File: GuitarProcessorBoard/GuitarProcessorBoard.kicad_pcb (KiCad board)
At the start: 4 copper layers, 86 x 65 mm, 126 parts, among them J301 SWD Header, J302 PWR, J304 MODE, J305 BYP, J307 ScopeGroundLoop, SW301 RST, SW302 BOOT, U1 AMS1117, U201 TLV320AIC3204, U202 TL074, U301 STM32H7B0VBT6, U302 TPS63070, U303 SSD1306_OLED_128x64, U304 74HC595, Y301 32MHz, Y302 32.768kHZ

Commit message: rev2 sent to fab
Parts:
- moved SW302 2.27 mm to (-162.4, 44.5)
- moved C211 0.55 mm to (-126.5, 52.1)
- moved C210 0.33 mm to (-122.9, 51.9)
- moved R206 0.25 mm to (-126.5, 48.0)
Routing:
- net BOOT0: track 11.1 -> 8.92 mm
- net +3.3V: track 353.2 -> 354.6 mm
- net Net-(U201-AVDD): track 2.54 -> 3.30 mm
- net Net-(U201-IN1_L): track 15.3 -> 14.7 mm
- net /MCU/LED_A6: track 18.8 -> 18.2 mm
- net GND: track 95.6 -> 95.2 mm, vias 92 -> 98

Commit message: new layout
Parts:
- removed C201, C208, C209, C210, C211, C214, C215, C216, C304, C306, C307, C309, C311, C312, C313, C318, C322, C332, C333: 100n, Capacitor_SMD:C_0805_2012Metric
- removed C202, C308, C310, C314: 2u2, Capacitor_SMD:C_0805_2012Metric
- removed C203, C204, C205, C206, C303, C319, C321, C323: 10u, Capacitor_SMD:C_0805_2012Metric
- removed C207, C212: 4n7, Capacitor_SMD:C_0805_2012Metric
- removed C301, C302: 10p, Capacitor_SMD:C_0805_2012Metric
- removed C315, C317: 6p, Capacitor_SMD:C_0805_2012Metric
- removed C324: 22u, Capacitor_SMD:C_0805_2012Metric
- removed C326: 330u, Capacitor_THT:CP_Radial_D5.0mm_P2.50mm
- removed C327, C328, C329: 10n, Capacitor_SMD:C_0805_2012Metric
- removed D301: RED, LED_THT:LED_D3.0mm
- removed D302, D308, D309, D310, D311, D312: ORANGE, LED_THT:LED_D3.0mm
- removed D304: PMEG3030, Diode_SMD:D_SOD-123
- removed D307: GREEN, LED_THT:LED_D3.0mm
- removed J301: SWD Header, Connector_PinHeader_2.54mm:PinHeader_1x06_P2.54mm_Vertical
- removed J302: PWR, Connector_PinHeader_2.54mm:PinHeader_1x04_P2.54mm_Vertical
- removed J304: MODE, Connector_PinHeader_2.54mm:PinHeader_1x02_P2.54mm_Vertical
- removed J305: BYP, Connector_PinHeader_2.54mm:PinHeader_1x02_P2.54mm_Vertical
- removed J307: ScopeGroundLoop, Connector:THT_GND_WIRE
- removed L301: 1u5, Inductor_SMD:L_Coilcraft_XAL4020-XXX
- removed R201, R305, R313: 47k, Resistor_SMD:R_0805_2012Metric
- removed R202, R203, R205, R209, R210, R211, R215, R309, R310, R312, R327, R328: 100k, Resistor_SMD:R_0805_2012Metric
- removed R204, R212, R216: 51k, Resistor_SMD:R_0805_2012Metric
- removed R206, R207: 470k, Resistor_SMD:R_0805_2012Metric
- removed R208, R214: 1k, Resistor_SMD:R_0805_2012Metric
- removed R220, R330, R331, R332, R333: 22, Resistor_SMD:R_0805_2012Metric
- removed R301, R302, R303, R304: 2k2, Resistor_SMD:R_0805_2012Metric
- removed R306, R307, R308, R318, R322, R323, R324, R325: 470, Resistor_SMD:R_0805_2012Metric
- removed R311: 10k, Resistor_SMD:R_0805_2012Metric
- removed R314: 5k1, Resistor_SMD:R_0805_2012Metric
- removed R315, R316, R317: 22k, Resistor_SMD:R_0805_2012Metric
- removed RV301, RV302, RV303: 100kB, Potentiometer_THT:Potentiometer_Alpha_RD901F-40-00D_Single_Vertical_CircularHoles
- removed SW301: RST, Button_Switch_SMD:SW_SPST_B3U-1000P
- removed SW302: BOOT, Button_Switch_SMD:SW_SPST_B3U-1000P
- removed TP301: In, TestPoint:TestPoint_THTPad_D2.0mm_Drill1.0mm_VAL
- removed TP302: Out, TestPoint:TestPoint_THTPad_D2.0mm_Drill1.0mm_VAL
- removed TP303: 3v3D, TestPoint:TestPoint_THTPad_D2.0mm_Drill1.0mm_VAL
- removed U201: TLV320AIC3204, Package_DFN_QFN:VQFN-32-1EP_5x5mm_P0.5mm_EP3.1x3.1mm
- removed U202: TL074, Package_SO:SOIC-14_3.9x8.7mm_P1.27mm
- removed U301: STM32H7B0VBT6, Package_QFP:LQFP-100_14x14mm_P0.5mm
- removed U302: TPS63070, Package_DFN_QFN:TXN_QFN15
- removed U303: SSD1306_OLED_128x64, Display:SSD1306_OLED_128x64_OffBoard
- removed U304: 74HC595, Package_SO:SOIC-16_3.9x9.9mm_P1.27mm
- removed Y301: 32MHz, Crystal:Crystal_SMD_EuroQuartz_MT-4Pin_3.2x2.5mm
- removed Y302: 32.768kHZ, Crystal:Crystal_SMD_SeikoEpson_MC306-4Pin_8.0x3.2mm
- added C10: 10u, Capacitor_SMD:C_0805_2012Metric, B.Cu at (-142.6, 83.1)
- added C11: 10u, Capacitor_SMD:C_0805_2012Metric, B.Cu at (-142.4, 77.5)
- added C12: 10u, Capacitor_SMD:C_0805_2012Metric, B.Cu at (-165.9, 81.7)
- added C13: 10u, Capacitor_SMD:C_0805_2012Metric, B.Cu at (-137.8, 89.8)
- added C14: 100n, Capacitor_SMD:C_0805_2012Metric, B.Cu at (-143.9, 79.0)
- added C15: 4n7, Capacitor_SMD:C_0805_2012Metric, B.Cu at (-150.1, 80.4)
- added C16: 4n7, Capacitor_SMD:C_0805_2012Metric, B.Cu at (-144.3, 86.9)
- added C17: 2u2, Capacitor_SMD:C_0805_2012Metric, B.Cu at (-139.1, 79.6)
- added C18: 100n, Capacitor_SMD:C_0805_2012Metric, B.Cu at (-146.9, 89.4)
- added C19: 100n, Capacitor_SMD:C_0805_2012Metric, B.Cu at (-151.2, 84.6)
- added C20: 10u, Capacitor_SMD:C_0805_2012Metric, B.Cu at (-130.1, 84.8)
- added C21: 1u, Capacitor_SMD:C_0805_2012Metric, B.Cu at (-150.9, 95.3)
- added C22: 1u, Capacitor_SMD:C_0805_2012Metric, B.Cu at (-162.0, 90.6)
- added C24: 10p, Capacitor_SMD:C_0805_2012Metric, B.Cu at (-119.9, 51.8)
- added C25: 10u, Capacitor_SMD:C_0805_2012Metric, B.Cu at (-173.0, 70.4)
- added C26: 10p, Capacitor_SMD:C_0805_2012Metric, B.Cu at (-124.2, 47.9)
- added C27: 100n, Capacitor_SMD:C_0805_2012Metric, B.Cu at (-153.8, 74.6)
- added C28: 100n, Capacitor_SMD:C_0805_2012Metric, B.Cu at (-127.5, 50.3)
- added C29: 100n, Capacitor_SMD:C_0805_2012Metric, B.Cu at (-130.0, 48.1)
- added C30: 100n, Capacitor_SMD:C_0805_2012Metric, B.Cu at (-147.1, 60.1)
- added C31: 2u2, Capacitor_SMD:C_0805_2012Metric, B.Cu at (-130.4, 72.0)
- added C32: 100n, Capacitor_SMD:C_0805_2012Metric, B.Cu at (-134.7, 72.1)
- added C33: 2u2, Capacitor_SMD:C_0805_2012Metric, B.Cu at (-146.3, 64.4)
- added C34: 100n, Capacitor_SMD:C_0805_2012Metric, B.Cu at (-122.3, 61.6)
- added C35: 100n, Capacitor_SMD:C_0805_2012Metric, B.Cu at (-137.6, 48.1)
- added C36: 100n, Capacitor_SMD:C_0805_2012Metric, B.Cu at (-123.5, 54.8)
- added C37: 330u, Capacitor_THT:CP_Radial_D5.0mm_P2.50mm, B.Cu at (-94.8, 88.5)
- added C40: 100n, Capacitor_SMD:C_0805_2012Metric, B.Cu at (-92.0, 82.1)
- added C41: 330u, Capacitor_THT:CP_Radial_D5.0mm_P2.50mm, B.Cu at (-119.6, 57.9)
- added C42: 100n, Capacitor_SMD:C_0805_2012Metric, B.Cu at (-92.0, 78.4)
- added C43: 1u, Capacitor_SMD:C_0805_2012Metric, B.Cu at (-109.0, 80.6)
- added C44: 10u, Capacitor_SMD:C_0805_2012Metric, B.Cu at (-102.2, 74.9)
- added C45: 10n, Capacitor_SMD:C_0805_2012Metric, B.Cu at (-157.0, 41.8)
- added C46: 10n, Capacitor_SMD:C_0805_2012Metric, B.Cu at (-113.5, 41.5)
- added C47: 10u, Capacitor_SMD:C_0805_2012Metric, B.Cu at (-167.5, 47.7)
- added C48: 10n, Capacitor_SMD:C_0805_2012Metric, B.Cu at (-106.2, 68.2)
- added C49: 10n, Capacitor_SMD:C_0805_2012Metric, B.Cu at (-135.4, 41.7)
- added C50: 10u, Capacitor_SMD:C_0805_2012Metric, B.Cu at (-167.6, 44.2)
- added C51: 100n, Capacitor_SMD:C_0805_2012Metric, B.Cu at (-175.3, 39.8)
- added C53: 10u, Capacitor_SMD:C_0805_2012Metric, B.Cu at (-168.3, 37.2)
- added C54: 22u, Capacitor_SMD:C_0805_2012Metric, B.Cu at (-168.3, 33.9)
- added C55: 330u, Capacitor_THT:CP_Radial_D5.0mm_P2.50mm, B.Cu at (-176.4, 47.0)
- added C56: 330u, Capacitor_THT:CP_Radial_D5.0mm_P2.50mm, B.Cu at (-108.9, 47.5)
- added C8: 100n, Capacitor_SMD:C_0805_2012Metric, B.Cu at (-114.0, 91.6)
- added C9: 10u, Capacitor_SMD:C_0805_2012Metric, B.Cu at (-112.6, 80.6)
- added D1: PMEG3030, Diode_SMD:D_SOD-123, B.Cu at (-97.7, 90.3)
- added D2: RED, LED_THT:LED_D3.0mm, F.Cu at (-144.0, 35.9)
- added D3: GREEN, LED_THT:LED_D3.0mm, F.Cu at (-122.2, 35.8)
- added D4: ORANGE, LED_THT:LED_D3.0mm, F.Cu at (-92.0, 36.2)
- added D5: ORANGE, LED_THT:LED_D3.0mm, F.Cu at (-92.0, 42.7)
- added D6: ORANGE, LED_THT:LED_D3.0mm, F.Cu at (-92.0, 49.2)
- added D7: ORANGE, LED_THT:LED_D3.0mm, F.Cu at (-92.0, 55.7)
- added D8: ORANGE, LED_THT:LED_D3.0mm, F.Cu at (-92.0, 62.2)
- added D9: ORANGE, LED_THT:LED_D3.0mm, F.Cu at (-92.0, 68.7)
- added J1: SWD Header, Connector_PinHeader_2.54mm:PinHeader_1x06_P2.54mm_Vertical, F.Cu at (-176.0, 54.3)
- added J2: IO, Connector_PinHeader_2.54mm:PinHeader_1x06_P2.54mm_Vertical, F.Cu at (-107.8, 98.1)
- added J3: ScopeGroundLoop, Capacitor_THT:THT_GND_WIRE, B.Cu at (-101.6, 37.4)
- added J4: MODE, Connector_PinHeader_2.54mm:PinHeader_1x02_P2.54mm_Vertical, B.Cu at (-176.1, 94.8)
- added J5: BYP, Connector_PinHeader_2.54mm:PinHeader_1x02_P2.54mm_Vertical, B.Cu at (-176.2, 87.0)
- added L1: 1u5, Inductor_SMD:L_Coilcraft_XAL4020-XXX, B.Cu at (-166.9, 40.7)
- added R1: 470k, Resistor_SMD:R_0805_2012Metric, B.Cu at (-117.7, 84.7)
- added R10: 22, Resistor_SMD:R_0805_2012Metric, B.Cu at (-130.7, 81.5)
- added R11: 100k, Resistor_SMD:R_0805_2012Metric, B.Cu at (-109.0, 77.3)
- added R12: 100k, Resistor_SMD:R_0805_2012Metric, B.Cu at (-112.6, 77.3)
- added R13: 100k, Resistor_SMD:R_0805_2012Metric, B.Cu at (-164.3, 83.2)
- added R14: 100k, Resistor_SMD:R_0805_2012Metric, B.Cu at (-161.8, 80.7)
- added R15: 1k, Resistor_SMD:R_0805_2012Metric, B.Cu at (-148.7, 81.9)
- added R16: 1k, Resistor_SMD:R_0805_2012Metric, B.Cu at (-145.8, 85.5)
- added R17: 470k, Resistor_SMD:R_0805_2012Metric, B.Cu at (-150.1, 91.3)
- added R18: 470k, Resistor_SMD:R_0805_2012Metric, B.Cu at (-158.5, 84.0)
- added R19: 470k, Resistor_SMD:R_0805_2012Metric, B.Cu at (-152.6, 93.8)
- added R2: 470k, Resistor_SMD:R_0805_2012Metric, B.Cu at (-110.9, 89.1)
- added R20: 470k, Resistor_SMD:R_0805_2012Metric, B.Cu at (-161.0, 86.5)
- added R21: 100k, Resistor_SMD:R_0805_2012Metric, B.Cu at (-167.8, 65.9)
- added R22: 100k, Resistor_SMD:R_0805_2012Metric, B.Cu at (-139.9, 50.6)
- added R23: 47k, Resistor_SMD:R_0805_2012Metric, B.Cu at (-159.0, 65.2)
- added R26: 22, Resistor_SMD:R_0805_2012Metric, B.Cu at (-121.6, 70.5)
- added R27: 22, Resistor_SMD:R_0805_2012Metric, B.Cu at (-114.1, 67.0)
- added R28: 22, Resistor_SMD:R_0805_2012Metric, B.Cu at (-118.1, 68.6)
- added R29: 22, Resistor_SMD:R_0805_2012Metric, B.Cu at (-115.1, 72.1)
- added R3: 470k, Resistor_SMD:R_0805_2012Metric, B.Cu at (-119.4, 97.3)
- added R30: 2k2, Resistor_SMD:R_0805_2012Metric, B.Cu at (-125.6, 82.5)
- added R31: 2k2, Resistor_SMD:R_0805_2012Metric, B.Cu at (-122.2, 83.5)
- added R32: 100k, Resistor_SMD:R_0805_2012Metric, B.Cu at (-172.4, 96.5)
- added R33: 100k, Resistor_SMD:R_0805_2012Metric, B.Cu at (-172.6, 88.6)
- added R34: 22k, Resistor_SMD:R_0805_2012Metric, B.Cu at (-154.6, 41.7)
- added R35: 22k, Resistor_SMD:R_0805_2012Metric, B.Cu at (-111.4, 41.6)
- added R36: 22k, Resistor_SMD:R_0805_2012Metric, B.Cu at (-104.1, 68.2)
- added R37: 22k, Resistor_SMD:R_0805_2012Metric, B.Cu at (-132.9, 41.7)
- added R38: 10k, Resistor_SMD:R_0805_2012Metric, B.Cu at (-171.2, 44.2)
- added R39: 47k, Resistor_SMD:R_0805_2012Metric, B.Cu at (-170.1, 78.4)
- added R4: 470k, Resistor_SMD:R_0805_2012Metric, B.Cu at (-110.8, 94.3)
- added R42: 100k, Resistor_SMD:R_0805_2012Metric, B.Cu at (-175.3, 42.1)
- added R43: 47k, Resistor_SMD:R_0805_2012Metric, B.Cu at (-172.0, 36.5)
- added R44: 15k, Resistor_SMD:R_0805_2012Metric, B.Cu at (-175.4, 36.5)
- added R45: 470, Resistor_SMD:R_0805_2012Metric, B.Cu at (-144.0, 41.7)
- added R46: 470, Resistor_SMD:R_0805_2012Metric, B.Cu at (-122.2, 41.4)
- added R47: 470, Resistor_SMD:R_0805_2012Metric, B.Cu at (-97.6, 36.2)
- added R48: 470, Resistor_SMD:R_0805_2012Metric, B.Cu at (-97.6, 42.5)
- added R49: 470, Resistor_SMD:R_0805_2012Metric, B.Cu at (-97.6, 49.6)
- added R5: 470k, Resistor_SMD:R_0805_2012Metric, B.Cu at (-124.6, 88.9)
- added R50: 470, Resistor_SMD:R_0805_2012Metric, B.Cu at (-97.6, 55.8)
- added R51: 470, Resistor_SMD:R_0805_2012Metric, B.Cu at (-97.8, 60.7)
- added R52: 470, Resistor_SMD:R_0805_2012Metric, B.Cu at (-97.8, 68.7)
- added R6: 470k, Resistor_SMD:R_0805_2012Metric, B.Cu at (-113.8, 88.4)
- added R7: 470k, Resistor_SMD:R_0805_2012Metric, B.Cu at (-124.5, 95.1)
- added R8: 470k, Resistor_SMD:R_0805_2012Metric, B.Cu at (-113.6, 95.2)
- added R9: 47k, Resistor_SMD:R_0805_2012Metric, B.Cu at (-134.2, 77.0)
- added RV1: 100kB, Potentiometer_THT:Potentiometer_Alpha_RD901F-40-00D_Single_Vertical_CircularHoles, F.Cu at (-157.1, 44.6)
- added RV2: 100kB, Potentiometer_THT:Potentiometer_Alpha_RD901F-40-00D_Single_Vertical_CircularHoles, F.Cu at (-113.9, 44.6)
- added RV3: 100kB, Potentiometer_THT:Potentiometer_Alpha_RD901F-40-00D_Single_Vertical_CircularHoles, F.Cu at (-106.5, 71.3)
- added RV4: 100kB, Potentiometer_THT:Potentiometer_Alpha_RD901F-40-00D_Single_Vertical_CircularHoles, F.Cu at (-135.5, 44.6)
- added SW1: RST, Button_Switch_SMD:SW_SPST_B3U-1000P, B.Cu at (-167.1, 63.2)
- added SW3: SW_1, Button_Switch_THT:MiniToggle_SPST, F.Cu at (-174.0, 75.9)
- added TP10: DACR, TestPoint:TestPoint_THTPad_D2.0mm_Drill1.0mm_VAL, B.Cu at (-154.2, 81.1)
- added TP2: InR, TestPoint:TestPoint_THTPad_D2.0mm_Drill1.0mm_VAL, B.Cu at (-100.5, 87.0)
- added TP3: 3v3D, TestPoint:TestPoint_THTPad_D2.0mm_Drill1.0mm_VAL, B.Cu at (-168.9, 54.2)
- added TP4: OutL, TestPoint:TestPoint_THTPad_D2.0mm_Drill1.0mm_VAL, B.Cu at (-146.4, 94.6)
- added TP5: OutR, TestPoint:TestPoint_THTPad_D2.0mm_Drill1.0mm_VAL, B.Cu at (-162.6, 95.4)
- added TP6: 3v3A, TestPoint:TestPoint_THTPad_D2.0mm_Drill1.0mm_VAL, B.Cu at (-105.2, 80.6)
- added TP7: DB1, TestPoint:TestPoint_THTPad_D2.0mm_Drill1.0mm_VAL, B.Cu at (-147.8, 55.6)
- added TP8: DB2, TestPoint:TestPoint_THTPad_D2.0mm_Drill1.0mm_VAL, B.Cu at (-144.8, 53.5)
- added TP9: DACL, TestPoint:TestPoint_THTPad_D2.0mm_Drill1.0mm_VAL, B.Cu at (-142.4, 90.4)
- added U2: TL072, Package_SO:SOIC-8_3.9x4.9mm_P1.27mm, B.Cu at (-156.8, 89.2)
- added U3: TLV320AIC3204, Package_DFN_QFN:VQFN-32-1EP_5x5mm_P0.5mm_EP3.1x3.1mm, B.Cu at (-136.4, 85.2)
- added U4: 74HC595, Package_SO:SOIC-16_3.9x9.9mm_P1.27mm, B.Cu at (-160.8, 71.4)
- added U5: STM32H7B0VBT6, Package_QFP:LQFP-100_14x14mm_P0.5mm, B.Cu at (-134.5, 60.2)
- added U6: AMS1117, Package_TO_SOT_SMD:SOT-223-3_TabPin2, B.Cu at (-98.8, 80.4)
- added U7: TPS63070, Converter_DCDC:TXN_QFN15, B.Cu at (-171.3, 40.7)
- added Y1: 32MHz, Crystal:Crystal_SMD_EuroQuartz_MT-4Pin_3.2x2.5mm, B.Cu at (-122.1, 49.9)
- C1, C3: value 330u -> 100n; footprint Capacitor_THT:CP_Radial_D5.0mm_P2.50mm -> Capacitor_SMD:C_0805_2012Metric
- C2, C7: value 10u -> 100n
- C6: value 1u -> 100n
- TP1: value 3v3A -> InL; moved to B.Cu
- U1: value AMS1117 -> TL074; footprint Package_TO_SOT_SMD:SOT-223-3_TabPin2 -> Package_SO:SOIC-14_3.9x8.7mm_P1.27mm
- moved C7 79.1 mm to (-157.1, 94.4), turned to -45 degrees
- moved C1 68.6 mm to (-105.5, 87.0)
- moved C5 63.3 mm to (-130.8, 92.4), turned to 180 degrees
- moved C4 62.2 mm to (-129.1, 88.1), turned to 180 degrees
- moved C6 59.5 mm to (-130.8, 94.6), turned to 180 degrees
- moved U1 57.5 mm to (-119.7, 91.6), turned to 180 degrees
- moved C2 52.4 mm to (-105.6, 89.7)
- moved TP1 46.2 mm to (-102.2, 89.8), turned to 180 degrees
- moved C3 37.6 mm to (-129.1, 90.2)
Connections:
- C1 pad 1: +3.3V -> IN_R
- C1 pad 2: GND -> Net-(C1-Pad2)
- C2 pad 1: +3.3VA -> IN_L
- C2 pad 2: GND -> Net-(C2-Pad2)
- C3 pad 1: +3.3VA -> /Audio/RightInputNeg
- C3 pad 2: GND -> /Audio/In1R
- C4 pad 1: GND -> /Audio/RightInputPos
- C4 pad 2: VCC -> /Audio/In1L
- C5 pad 1: GND -> /Audio/LeftInputNeg
- C5 pad 2: +3.3VA -> /Audio/In2L
- C6 pad 1: +3.3VA -> /Audio/LeftInputPos
- C6 pad 2: GND -> /Audio/In2R
- C7 pad 1: +3.3VA -> VCC
- TP1 pad 1: +3.3VA -> IN_L
- U1 pad 1: GND -> /Audio/RightInputPos
- U1 pad 2: +3.3VA -> Net-(U1A--)
- U1 pad 3: VCC -> /Audio/Bias1
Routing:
- net +3.3V: track 354.6 -> 0.00 mm, vias 5 -> 0
- net VCC: track 196.9 -> 0.00 mm, vias 1 -> 0
- net +3.3VA: track 161.5 -> 0.00 mm, vias 5 -> 0
- net ADC_C: track 109.1 -> 0.00 mm, vias 2 -> 0
- net GND: track 95.2 -> 0.00 mm, vias 98 -> 0
- net FX_IN: track 85.8 -> 0.00 mm, vias 3 -> 0
- net LED_DATA: track 79.0 -> 0.00 mm, vias 1 -> 0
- net ADC_B: track 75.1 -> 0.00 mm, vias 2 -> 0
- net LED_NRST: track 73.3 -> 0.00 mm, vias 1 -> 0
- net FX_OUT: track 73.0 -> 0.00 mm, vias 2 -> 0
- net LED_LATCH: track 71.3 -> 0.00 mm, vias 1 -> 0
- net LED_SCK: track 68.6 -> 0.00 mm, vias 1 -> 0
- net NRST: track 64.4 -> 0.00 mm, vias 1 -> 0
- net /MCU/LED_BYPASS: track 62.3 -> 0.00 mm
- net BYP_BTN: track 54.8 -> 0.00 mm, vias 1 -> 0
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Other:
- board size 86 x 65 mm -> 88.7 x 70 mm
- board text added: "INL"
- board text added: "INR"
- board text added: "OUTL"
- board text added: "OUTR"
- board text added: "Rev 3- 04/2026 Hayden Setlik"
- board text removed: "Bypass"
- board text removed: "IN"
- board text removed: "OUT"
- board text removed: "Rev 2- 01/2026 Hayden Setlik"
- board text removed: "Tempo"

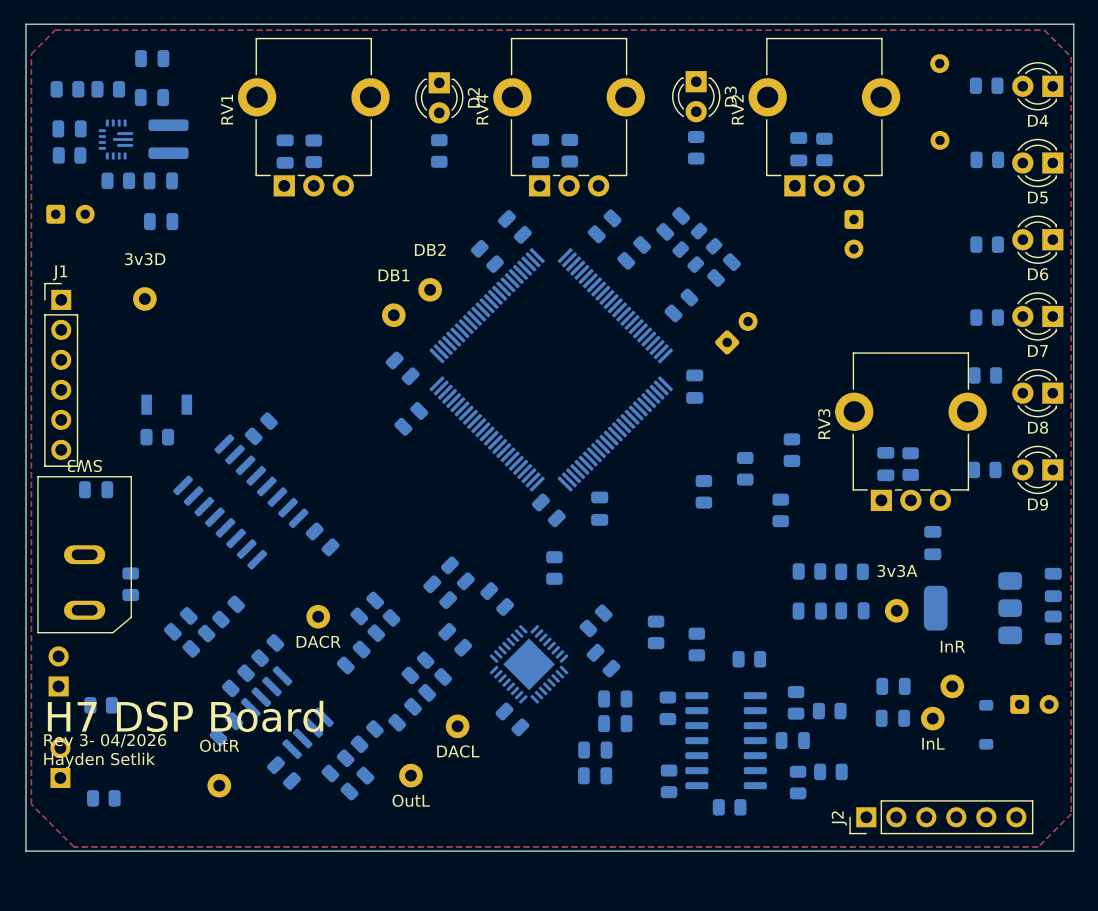
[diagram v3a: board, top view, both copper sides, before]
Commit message: prelim. routing, DRC passing
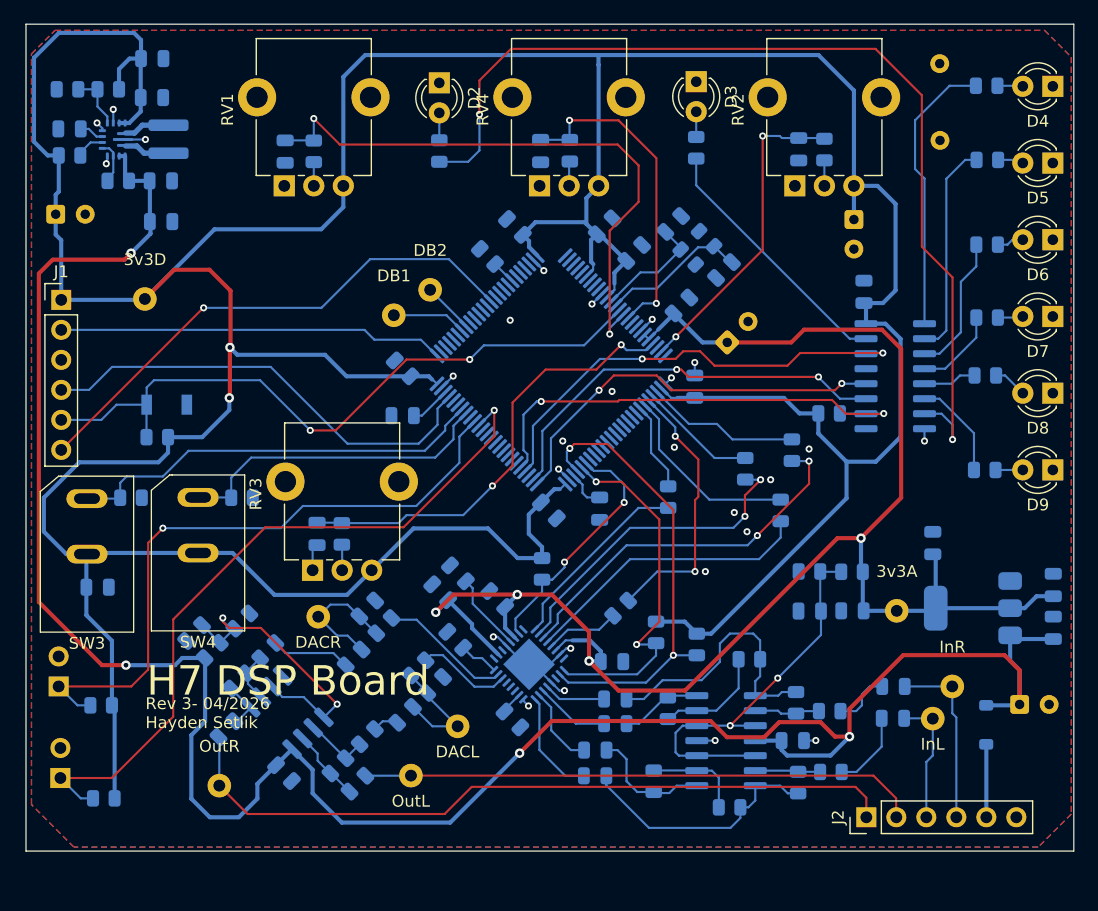
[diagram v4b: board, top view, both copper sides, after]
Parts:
- added R40: 47k, Resistor_SMD:R_0805_2012Metric, B.Cu at (-160.7, 71.0)
- added SW4: SW_2, Button_Switch_THT:MiniToggle_SPST, F.Cu at (-164.4, 75.7)
- moved U4 56.4 mm to (-105.4, 60.8), turned to 180 degrees
- moved C27 50.4 mm to (-108.0, 53.6), turned to 90 degrees
- moved C48 48.5 mm to (-154.3, 74.1)
- moved R36 48.5 mm to (-152.2, 74.1)
- moved RV3 48.5 mm to (-154.7, 77.2)
- moved R23 48.1 mm to (-111.0, 63.9), turned to 0 degrees
- moved C25 8.25 mm to (-172.9, 78.6)
- moved R39 7.33 mm to (-170.1, 71.0), turned to 0 degrees
- moved R26 3.06 mm to (-124.6, 71.0)
- moved R10 2.34 mm to (-128.6, 80.4)
- moved C12 1.37 mm to (-164.7, 82.5)
- moved R13 1.37 mm to (-163.2, 84.0)
- moved R14 1.37 mm to (-160.7, 81.5)
- moved R7 1.30 mm to (-125.8, 95.0), turned to 90 degrees
- moved R9 1.05 mm to (-135.3, 77.1)
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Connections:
- J2 pad 1: OUT_L -> OUT_R
- J2 pad 2: OUT_R -> OUT_L
- R7 pad 1: Net-(U1C--) -> /Audio/LeftInputNeg
- R7 pad 2: /Audio/LeftInputNeg -> Net-(U1C--)
- R9 pad 1: +3.3VA -> +3.3V
- U4 pad 1: /MCU/LED_A5 -> /MCU/LED_A1
- U4 pad 15: /MCU/LED_A6 -> /MCU/LED_BYPASS
- U4 pad 2: /MCU/LED_A4 -> /MCU/LED_A2
- U4 pad 4: /MCU/LED_A2 -> /MCU/LED_A4
- U4 pad 5: /MCU/LED_A1 -> /MCU/LED_A5
- U4 pad 6: /MCU/LED_BYPASS -> /MCU/LED_A6
- U5 pad 53: LED_NRST -> unconnected-(U5-PB14-Pad53)
- U5 pad 55: unconnected-(U5-PD8-Pad55) -> LED_NRST
- U5 pad 65: unconnected-(U5-PC8-Pad65) -> MODE_BTN
- U5 pad 66: SWITCH1 -> BYP_BTN
- U5 pad 68: BYP_BTN -> SWITCH2
- U5 pad 69: MODE_BTN -> SWITCH1
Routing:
- net +3.3V: track 0.00 -> 389.8 mm, vias 0 -> 2
- net VCC: track 0.00 -> 189.5 mm, vias 0 -> 4
- net +3.3VA: track 0.00 -> 135.3 mm, vias 0 -> 4
- net /MCU/LED_TEMPO: track 0.00 -> 84.1 mm, vias 0 -> 2
- net OUT_R: track 0.00 -> 62.9 mm
- net MODE_BTN: track 0.00 -> 61.1 mm, vias 0 -> 1
- net NRST: track 0.00 -> 58.2 mm, vias 0 -> 2
- net BYP_BTN: track 0.00 -> 55.4 mm, vias 0 -> 1
- net ADC_C: track 0.00 -> 50.9 mm, vias 0 -> 2
- net OUT_L: track 0.00 -> 47.3 mm
- net SWO: track 0.00 -> 44.6 mm, vias 0 -> 1
- net LED_NRST: track 0.00 -> 40.1 mm, vias 0 -> 2
- net SWDIO: track 0.00 -> 38.8 mm
- net CODEC_SDA: track 0.00 -> 38.8 mm, vias 0 -> 2
- net LED_DATA: track 0.00 -> 38.8 mm, vias 0 -> 2
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
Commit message: minor tweaks
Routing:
- net GND: track 31.7 -> 36.9 mm, vias 27 -> 31
- net OUT_R: track 62.9 -> 60.0 mm
- net ADC_C: track 50.9 -> 52.6 mm

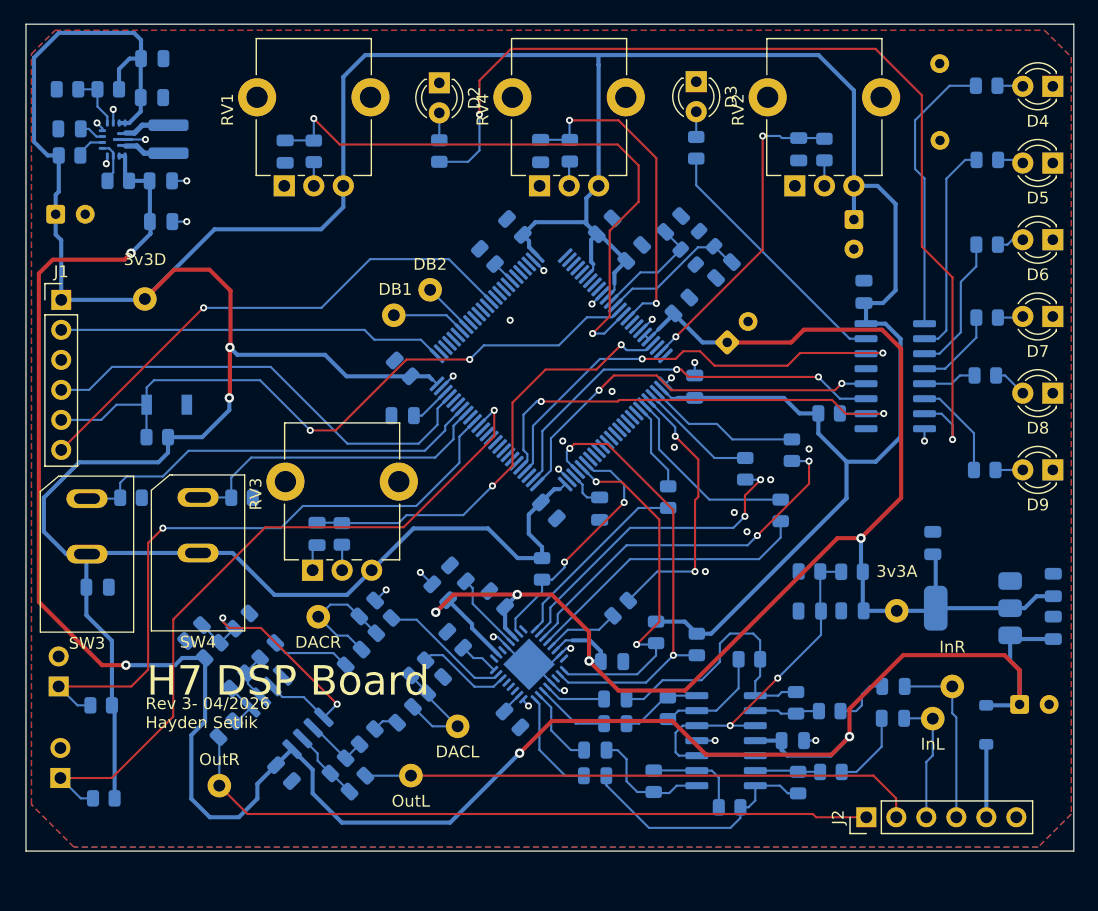
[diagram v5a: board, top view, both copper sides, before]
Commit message: new layout, pinout switcharoo
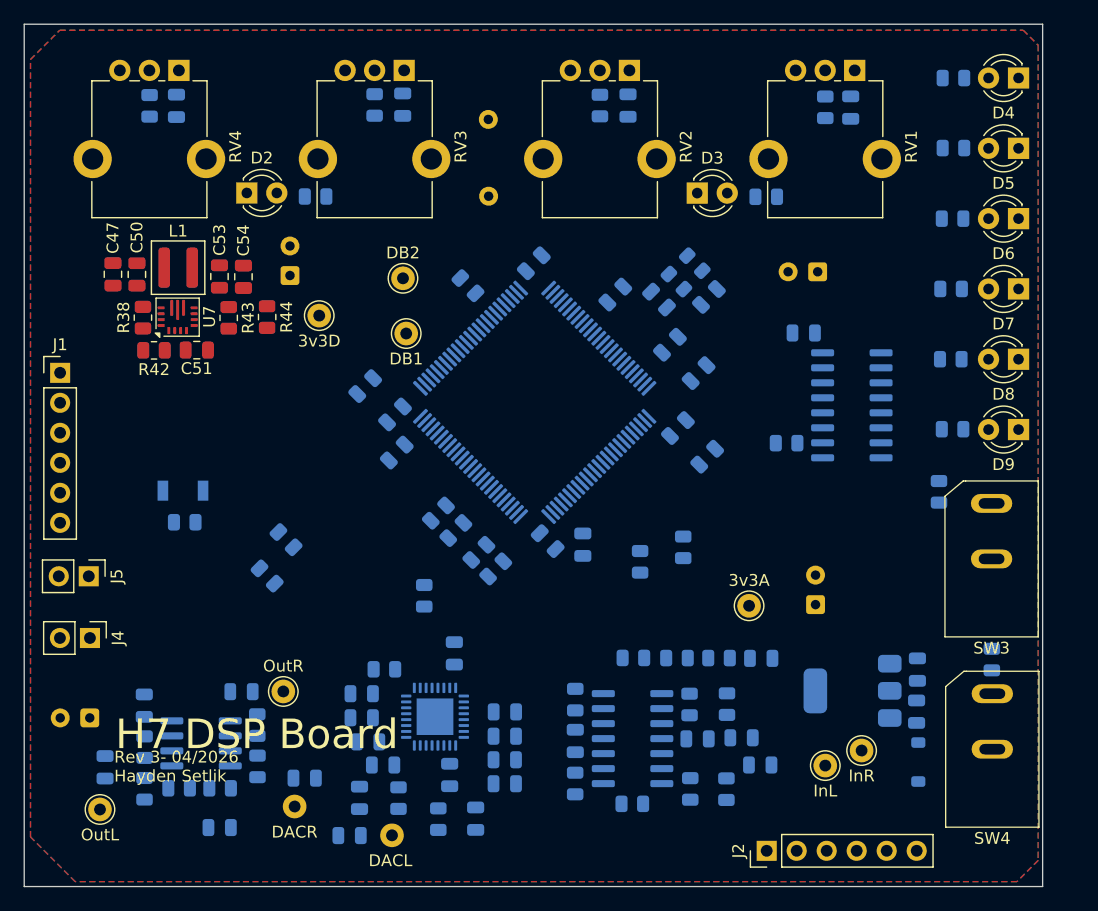
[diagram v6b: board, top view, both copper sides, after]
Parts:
- removed R26: 22, Resistor_SMD:R_0805_2012Metric
- added R41: 22, Resistor_SMD:R_0805_2012Metric, B.Cu at (-144.1, 72.3)
- C47, C50, C51, C53, C54, J4, J5, L1, R38, R42, R43, R44, TP1, TP2, TP3, TP4, TP5, TP6, TP7, TP8: moved to F.Cu
- J3: footprint Capacitor_THT:THT_GND_WIRE -> Connector:THT_GND_WIRE
- U7: footprint Converter_DCDC:TXN_QFN15 -> Converter_DCDC:Converter_DCDC_TXN_QFN15; moved to F.Cu
- moved C37 78.7 mm to (-173.6, 89.7), turned to 180 degrees
- moved SW3 76.6 mm to (-97.2, 76.2)
- moved SW4 69.3 mm to (-97.2, 92.3)
- moved R39 68.4 mm to (-101.7, 70.5), turned to 90 degrees
- moved R40 64.9 mm to (-97.2, 84.8), turned to 90 degrees
- moved C25 52.8 mm to (-121.3, 67.6), turned to 45 degrees
- moved RV1 49.3 mm to (-108.8, 34.9), turned to -90 degrees
- moved C45 48.0 mm to (-109.2, 38.0), turned to 90 degrees
- moved R34 43.5 mm to (-111.3, 38.0), turned to -90 degrees
- moved RV3 43.0 mm to (-146.9, 34.9), turned to -90 degrees
- moved J3 38.5 mm to (-139.8, 42.1)
- moved C48 37.1 mm to (-147.1, 37.8), turned to 90 degrees
- moved R36 36.4 mm to (-149.4, 37.8), turned to -90 degrees
- moved R37 35.8 mm to (-168.5, 37.9), turned to -90 degrees
- moved RV4 32.1 mm to (-166.0, 34.9), turned to -90 degrees
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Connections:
- R27 pad 1: Net-(U5-PA4) -> Net-(U5-PB12)
- R28 pad 1: Net-(U5-PA5) -> Net-(U5-PB13)
- R29 pad 1: Net-(U5-PA7) -> Net-(U5-PB15)
- R9 pad 1: +3.3V -> +3.3VA
- SW3 pad 2: +3.3V -> +3.3VA
- SW4 pad 2: +3.3V -> +3.3VA
- U5 pad 28: Net-(U5-PA4) -> LED_LATCH
- U5 pad 29: Net-(U5-PA5) -> LED_SCK
- U5 pad 30: I2S_SDI -> unconnected-(U5-PA6-Pad30)
- U5 pad 31: Net-(U5-PA7) -> LED_DATA
- U5 pad 32: Net-(U5-PC4) -> LED_NRST
- U5 pad 36: unconnected-(U5-PB2-Pad36) -> SWITCH1
- U5 pad 37: unconnected-(U5-PE7-Pad37) -> SWITCH2
- U5 pad 51: LED_LATCH -> Net-(U5-PB12)
- U5 pad 52: LED_SCK -> Net-(U5-PB13)
- U5 pad 53: unconnected-(U5-PB14-Pad53) -> I2S_SDI
- U5 pad 54: LED_DATA -> Net-(U5-PB15)
- U5 pad 55: LED_NRST -> unconnected-(U5-PD8-Pad55)
- U5 pad 63: unconnected-(U5-PC6-Pad63) -> Net-(U5-PC6)
- U5 pad 68: SWITCH2 -> unconnected-(U5-PA9-Pad68)
- U5 pad 69: SWITCH1 -> unconnected-(U5-PA10-Pad69)
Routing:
- net +3.3V: track 389.8 -> 0.00 mm, vias 2 -> 0
- net VCC: track 189.7 -> 0.00 mm, vias 4 -> 0
- net +3.3VA: track 135.3 -> 0.00 mm, vias 4 -> 0
- net /MCU/LED_TEMPO: track 84.1 -> 0.00 mm, vias 2 -> 0
- net MODE_BTN: track 61.1 -> 0.00 mm, vias 1 -> 0
- net OUT_R: track 60.0 -> 0.00 mm
- net NRST: track 58.2 -> 0.00 mm, vias 2 -> 0
- net BYP_BTN: track 55.4 -> 0.00 mm, vias 1 -> 0
- net ADC_C: track 52.6 -> 0.00 mm, vias 2 -> 0
- net OUT_L: track 47.3 -> 0.00 mm
- net SWO: track 44.6 -> 0.00 mm, vias 1 -> 0
- net LED_NRST: track 40.1 -> 0.00 mm, vias 2 -> 0
- net SWDIO: track 38.8 -> 0.00 mm
- net CODEC_SDA: track 38.8 -> 0.00 mm, vias 2 -> 0
- net LED_DATA: track 38.8 -> 0.00 mm, vias 2 -> 0
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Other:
- board size 88.7 x 70 mm -> 86.2 x 73 mm
- board text removed: "ALG"
- board text removed: "BYP"
